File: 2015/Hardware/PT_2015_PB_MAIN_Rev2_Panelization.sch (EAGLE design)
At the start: 161 parts, among them Q1 Q_ACS711LC_SKETCH, Q11 Q_IRFS7437PbF, Q12 2N7002, Q14 Q_IRFS7437PbF, Q16 Q_IRFS7437PbF, Q18 Q_FDT86102LZ, Q20 Q_IRFS7437PbF, Q4 Q_ACS711LC, Q5 Q_ACS711LC, Q6 Q_IRFS7437PbF, Q7 Q_IRFS7437PbF, Q9 Q_IRFS7437PbF

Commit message: Fixed the Ferrite Bead Footprint
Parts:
- L3: device resistor:L-USL3216C -> rcl:L-USL4532C
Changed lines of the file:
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@@
 <part name="GND30" library="SparkFun-Aesthetics" deviceset="GND" device=""/>
 <part name="C17" library="resistor" deviceset="C-US" device="C1206" value="47µF"/>
-<part name="L3" library="resistor" deviceset="L-US" device="L3216C"/>
 <part name="C18" library="resistor" deviceset="C-US" device="C1206" value="47µF"/>
 <part name="GND31" library="SparkFun-Aesthetics" deviceset="GND" device=""/>
@@
 <part name="GND101" library="SparkFun-Aesthetics" deviceset="GND" device=""/>
 <part name="GND102" library="SparkFun-Aesthetics" deviceset="GND" device=""/>
+<part name="L3" library="rcl" deviceset="L-US" device="L4532C"/>
 </parts>
 <sheets>
@@
 <instance part="GND30" gate="1" x="218.44" y="116.84"/>
 <instance part="C17" gate="G$1" x="231.14" y="127"/>
-<instance part="L3" gate="G$1" x="241.3" y="129.54" rot="R90"/>
 <instance part="C18" gate="G$1" x="251.46" y="127"/>
 <instance part="GND31" gate="1" x="251.46" y="116.84"/>
@@
 <instance part="SG1" gate="G$1" x="-297.18" y="-165.1"/>
 <instance part="GND93" gate="1" x="-289.56" y="-180.34" rot="MR0"/>
+<instance part="L3" gate="G$1" x="241.3" y="129.54" rot="R90"/>
 </instances>
 <busses>
@@
 </segment>
 <segment>
-<pinref part="L3" gate="G$1" pin="2"/>
 <pinref part="C18" gate="G$1" pin="1"/>
 <wire x1="251.46" y1="129.54" x2="248.92" y2="129.54" width="0.1524" layer="91"/>
@@
 <wire x1="264.16" y1="129.54" x2="269.24" y2="129.54" width="0.1524" layer="91"/>
 <label x="269.24" y="129.54" size="1.27" layer="95" xref="yes"/>
-</segment>
-<segment>
+<pinref part="L3" gate="G$1" pin="2"/>
+</segment>
+<segment>

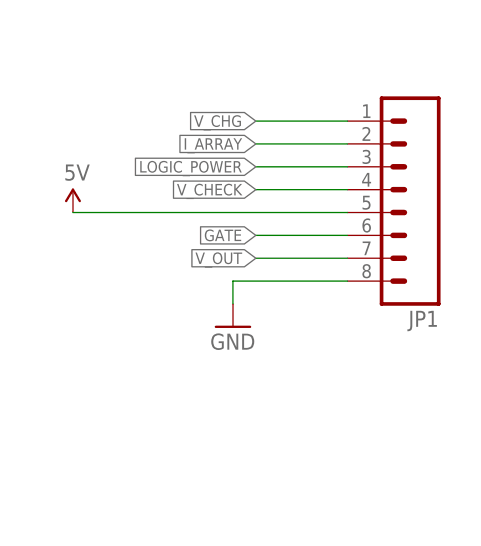
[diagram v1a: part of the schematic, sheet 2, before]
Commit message: Fixed the connector on SSR portion
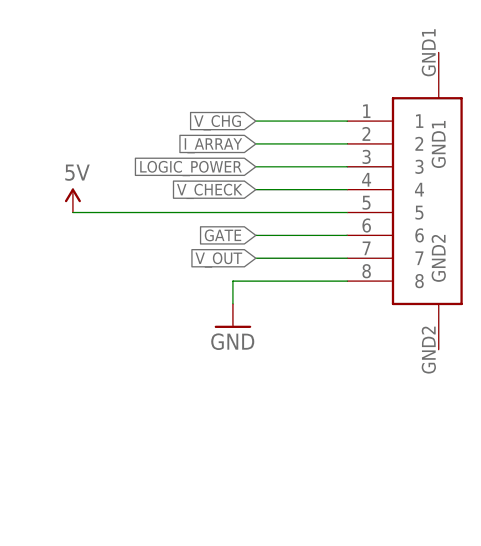
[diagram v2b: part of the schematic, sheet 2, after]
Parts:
- removed JP1: (no value), SparkFun-Connectors:M08BM08B-SRSS-TB
- added U$24: 8POS_LOGIC, New:8POS_LOGIC
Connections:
- net 5V_SSR: now also U$24.5; no longer JP1.5
- net GATE: now also U$24.6; no longer JP1.6
- net GND: now also U$24.8; no longer JP1.8
- net I_ARRAY: now also U$24.2; no longer JP1.2
- net LOGIC_POWER: now also U$24.3; no longer JP1.3
- net V_CHECK: now also U$24.4; no longer JP1.4
- net V_CHG: now also U$24.1; no longer JP1.1
- net V_OUT: now also U$24.7; no longer JP1.7
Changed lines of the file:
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@@
 <part name="D3" library="MRDT-2015-BMS" deviceset="D_STPS5045S" device=""/>
 <part name="IRLS3034-7P" library="MRDT-2015-BMS" deviceset="IRLS3034-7P" device=""/>
-<part name="JP1" library="SparkFun-Connectors" deviceset="M08" device="BM08B-SRSS-TB"/>
 <part name="SUPPLY17" library="SparkFun-Aesthetics" deviceset="5V" device=""/>
 <part name="GND100" library="SparkFun-Aesthetics" deviceset="GND" device=""/>
@@
 <part name="GND102" library="SparkFun-Aesthetics" deviceset="GND" device=""/>
 <part name="L3" library="rcl" deviceset="L-US" device="L4532C"/>
+<part name="U$24" library="New" deviceset="8POS_LOGIC" device=""/>
 </parts>
 <sheets>
@@
 <instance part="D3" gate="G$1" x="68.58" y="63.5" rot="R270"/>
 <instance part="IRLS3034-7P" gate="G$1" x="139.7" y="45.72" rot="R90"/>
-<instance part="JP1" gate="G$1" x="215.9" y="104.14" rot="R180"/>
 <instance part="SUPPLY17" gate="G$1" x="180.34" y="101.6"/>
 <instance part="GND100" gate="1" x="198.12" y="88.9"/>
@@
 <instance part="GND101" gate="1" x="116.84" y="50.8"/>
 <instance part="GND102" gate="1" x="81.28" y="50.8"/>
+<instance part="U$24" gate="G$1" x="215.9" y="96.52"/>
 </instances>
 <busses>
@@
 </segment>
 <segment>
-<pinref part="JP1" gate="G$1" pin="5"/>
 <wire x1="210.82" y1="101.6" x2="180.34" y2="101.6" width="0.1524" layer="91"/>
 <pinref part="SUPPLY17" gate="G$1" pin="5V"/>
+<pinref part="U$24" gate="G$1" pin="5"/>
 </segment>
 </net>
@@
 </segment>
 <segment>
-<pinref part="JP1" gate="G$1" pin="8"/>
 <wire x1="210.82" y1="93.98" x2="198.12" y2="93.98" width="0.1524" layer="91"/>
 <wire x1="198.12" y1="93.98" x2="198.12" y2="91.44" width="0.1524" layer="91"/>
 <pinref part="GND100" gate="1" pin="GND"/>
+<pinref part="U$24" gate="G$1" pin="8"/>
 </segment>
 <segment>
@@
 </segment>
 <segment>
-<pinref part="JP1" gate="G$1" pin="6"/>
 <wire x1="210.82" y1="99.06" x2="200.66" y2="99.06" width="0.1524" layer="91"/>
 <label x="200.66" y="99.06" size="1.27" layer="95" rot="R180" xref="yes"/>
+<pinref part="U$24" gate="G$1" pin="6"/>
 </segment>
 </net>
@@
 </segment>
 <segment>
-<pinref part="JP1" gate="G$1" pin="2"/>
 <wire x1="210.82" y1="109.22" x2="200.66" y2="109.22" width="0.1524" layer="91"/>
 <label x="200.66" y="109.22" size="1.27" layer="95" rot="R180" xref="yes"/>
+<pinref part="U$24" gate="G$1" pin="2"/>
 </segment>
 </net>
@@
 </segment>
 <segment>
-<pinref part="JP1" gate="G$1" pin="7"/>
 <wire x1="210.82" y1="96.52" x2="200.66" y2="96.52" width="0.1524" layer="91"/>
 <label x="200.66" y="96.52" size="1.27" layer="95" rot="R180" xref="yes"/>
+<pinref part="U$24" gate="G$1" pin="7"/>
 </segment>
 </net>
@@
 </segment>
 <segment>
-<pinref part="JP1" gate="G$1" pin="4"/>
 <wire x1="210.82" y1="104.14" x2="200.66" y2="104.14" width="0.1524" layer="91"/>
 <label x="200.66" y="104.14" size="1.27" layer="95" rot="R180" xref="yes"/>
+<pinref part="U$24" gate="G$1" pin="4"/>
 </segment>
 </net>
@@
 </segment>
 <segment>
-<pinref part="JP1" gate="G$1" pin="1"/>
 <wire x1="210.82" y1="111.76" x2="200.66" y2="111.76" width="0.1524" layer="91"/>
 <label x="200.66" y="111.76" size="1.27" layer="95" rot="R180" xref="yes"/>
+<pinref part="U$24" gate="G$1" pin="1"/>
 </segment>
 </net>
@@
 </segment>
 <segment>
-<pinref part="JP1" gate="G$1" pin="3"/>
 <wire x1="210.82" y1="106.68" x2="200.66" y2="106.68" width="0.1524" layer="91"/>
 <label x="200.66" y="106.68" size="1.27" layer="95" rot="R180" xref="yes"/>
-</segment>
-</net>
+<pinref part="U$24" gate="G$1" pin="3"/>
+</segment>
+</net>

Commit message: Switched out the SSR to meet 3oz Spec
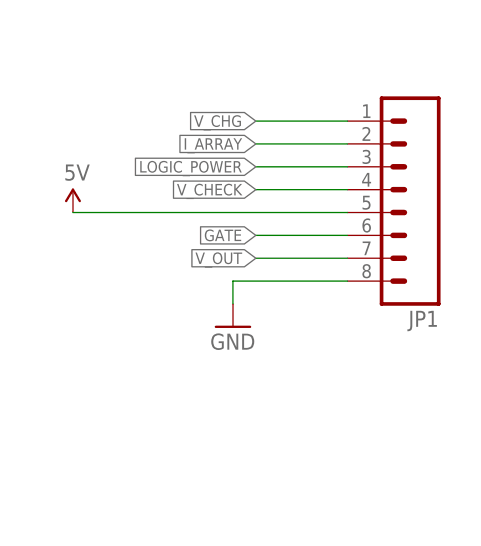
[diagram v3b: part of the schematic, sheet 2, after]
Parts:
- removed U$24: 8POS_LOGIC, New:8POS_LOGIC
- added JP1: (no value), SparkFun-Connectors:M08BM08B-SRSS-TB
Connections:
- removed net GND: 12V-AUX.L, 12V-CRIT.L, 5V-EXT.L, 5V-INT.L, ARM_P.L, AUX_P.L, BATT-NEG.P$1, C1.-, C10.1, C11.2, C12.2, C13.1, C14.1, C15.1, C16.1, C17.2, C18.2, C19.2, C2.-, C20.2, C21.-, C22.-, C23.1, C24.1, C25.1, C26.1, C27.2, C28.1, C29.1, C3.-, C30.1, C31.2, C32.1, C33.1, C34.1, C35.2, C36.1, C37.2, C38.2, C39.1, C4.-, C40.2, C41.1, C42.2, C43.2, C44.2, C45.-, C46.2, C5.1, C6.1, C7.2, C8.2, C9.2, CHARGER_IN.R, D1.A, D2.A, DOOKU-12V-CRIT.GND, DOOKU-12V-CRIT.GND1, LED1.C, LED10.C, LED11.C, LED12.C, LED13.C, LED14.C, LED2.C, LED3.C, LED4.C, LED5.C, LED6.C, LED7.C, LED8.C, LED9.C, MOTOR_1.L, MOTOR_2.L, MOTOR_3.L, MOTOR_4.L, MOTOR_5.L, MOTOR_6.L, OKI-78SR-5/1.5-W36H.GND, PALPATINE-12V.-VIN, PALPATINE-12V.-VOUT, Q1.GND, Q12.S, Q4.GND, Q5.GND, R17.2, R19.2, R23.2, R27.1, R4.1, R7.1, R8.1, SG1.1, SIDEOUS-12V.-VIN, SIDEOUS-12V.-VOUT, U$1.GND@1, U$1.GND@2, U$10.GND, U$11.GND, U$12.GND, U$13.GND, U$14.GND, U$15.GND, U$16.GND, U$17.GND, U$18.GND, U$19.GND, U$2.A, U$20.GND, U$21.GND, U$22.GND, U$23.GND, U$24.8, U$3.GND, U$4.7, U$4.8, U$5.A, U$6.GND, U$7.GND, U$8.GND, U$9.GND, VADER-5V-EXT.GND, VADER-5V-EXT.GND1
- new net 0: 12V-AUX.L, 12V-CRIT.L, 5V-EXT.L, 5V-INT.L, ARM_P.L, AUX_P.L, BATT-NEG.P$1, C1.-, C10.1, C11.2, C12.2, C13.1, C14.1, C15.1, C16.1, C17.2, C18.2, C19.2, C2.-, C20.2, C21.-, C22.-, C23.1, C24.1, C25.1, C26.1, C27.2, C28.1, C29.1, C3.-, C30.1, C31.2, C32.1, C33.1, C34.1, C35.2, C36.1, C37.2, C38.2, C39.1, C4.-, C40.2, C41.1, C42.2, C43.2, C44.2, C45.-, C5.1, C6.1, C7.2, C8.2, C9.2, D1.A, D2.A, DOOKU-12V-CRIT.GND, DOOKU-12V-CRIT.GND1, LED1.C, LED10.C, LED11.C, LED12.C, LED13.C, LED14.C, LED2.C, LED3.C, LED4.C, LED5.C, LED6.C, LED7.C, LED8.C, LED9.C, MOTOR_1.L, MOTOR_2.L, MOTOR_3.L, MOTOR_4.L, MOTOR_5.L, MOTOR_6.L, OKI-78SR-5/1.5-W36H.GND, PALPATINE-12V.-VIN, PALPATINE-12V.-VOUT, Q1.GND, Q12.S, Q4.GND, Q5.GND, R4.1, R7.1, R8.1, SG1.1, SIDEOUS-12V.-VIN, SIDEOUS-12V.-VOUT, U$1.GND@1, U$1.GND@2, U$10.GND, U$11.GND, U$12.GND, U$13.GND, U$14.GND, U$15.GND, U$16.GND, U$17.GND, U$18.GND, U$19.GND, U$2.A, U$20.GND, U$21.GND, U$3.GND, U$4.7, U$4.8, U$5.A, U$6.GND, U$7.GND, U$8.GND, U$9.GND, VADER-5V-EXT.GND, VADER-5V-EXT.GND1
- new net GND_SSR: C46.2, CHARGER_IN.R, JP1.8, R17.2, R19.2, R23.2, R27.1, U$22.GND, U$23.GND
- net 5V_SSR: now also JP1.5; no longer U$24.5
- net GATE: now also JP1.6; no longer U$24.6
- net I_ARRAY: now also JP1.2; no longer U$24.2
- net LOGIC_POWER: now also JP1.3; no longer U$24.3
- net V_CHECK: now also JP1.4; no longer U$24.4
- net V_CHG: now also JP1.1; no longer U$24.1
- net V_OUT: now also JP1.7; no longer U$24.7
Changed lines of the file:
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@@
 <part name="SG1" library="SparkFun-Electromechanical" deviceset="BUZZER" device="SMD2"/>
 <part name="GND93" library="SparkFun-Aesthetics" deviceset="GND" device=""/>
+<part name="L3" library="rcl" deviceset="L-US" device="L4532C"/>
 <part name="U$22" library="MRDT-2015-BMS" deviceset="ACS770" device=""/>
 <part name="IRLS3034-7P.2" library="MRDT-2015-BMS" deviceset="IRLS3034-7P" device=""/>
@@
 <part name="D3" library="MRDT-2015-BMS" deviceset="D_STPS5045S" device=""/>
 <part name="IRLS3034-7P" library="MRDT-2015-BMS" deviceset="IRLS3034-7P" device=""/>
+<part name="JP1" library="SparkFun-Connectors" deviceset="M08" device="BM08B-SRSS-TB"/>
 <part name="SUPPLY17" library="SparkFun-Aesthetics" deviceset="5V" device=""/>
 <part name="GND100" library="SparkFun-Aesthetics" deviceset="GND" device=""/>
@@
 <part name="GND101" library="SparkFun-Aesthetics" deviceset="GND" device=""/>
 <part name="GND102" library="SparkFun-Aesthetics" deviceset="GND" device=""/>
-<part name="L3" library="rcl" deviceset="L-US" device="L4532C"/>
-<part name="U$24" library="New" deviceset="8POS_LOGIC" device=""/>
 </parts>
 <sheets>
@@
 </busses>
 <nets>
-<net name="GND" class="0">
+<net name="0" class="0">
 <segment>
 <pinref part="DOOKU-12V-CRIT" gate="G$1" pin="GND"/>
@@
 <instance part="D3" gate="G$1" x="68.58" y="63.5" rot="R270"/>
 <instance part="IRLS3034-7P" gate="G$1" x="139.7" y="45.72" rot="R90"/>
+<instance part="JP1" gate="G$1" x="215.9" y="104.14" rot="R180"/>
 <instance part="SUPPLY17" gate="G$1" x="180.34" y="101.6"/>
 <instance part="GND100" gate="1" x="198.12" y="88.9"/>
@@
 <instance part="GND101" gate="1" x="116.84" y="50.8"/>
 <instance part="GND102" gate="1" x="81.28" y="50.8"/>
-<instance part="U$24" gate="G$1" x="215.9" y="96.52"/>
 </instances>
 <busses>
 </busses>
 <nets>
-<net name="N$354" class="0">
+<net name="N$33" class="0">
 <segment>
 <pinref part="IRLS3034-7P.2" gate="G$1" pin="SOURCE"/>
@@
 </segment>
 <segment>
+<pinref part="JP1" gate="G$1" pin="5"/>
 <wire x1="210.82" y1="101.6" x2="180.34" y2="101.6" width="0.1524" layer="91"/>
 <pinref part="SUPPLY17" gate="G$1" pin="5V"/>
-<pinref part="U$24" gate="G$1" pin="5"/>
-</segment>
-</net>
-<net name="GND" class="0">
+</segment>
+</net>
+<net name="GND_SSR" class="0">
 <segment>
 <pinref part="U$22" gate="G$1" pin="GND"/>
@@
 </segment>
 <segment>
+<pinref part="JP1" gate="G$1" pin="8"/>
 <wire x1="210.82" y1="93.98" x2="198.12" y2="93.98" width="0.1524" layer="91"/>
 <wire x1="198.12" y1="93.98" x2="198.12" y2="91.44" width="0.1524" layer="91"/>
 <pinref part="GND100" gate="1" pin="GND"/>
-<pinref part="U$24" gate="G$1" pin="8"/>
 </segment>
 <segment>
@@
 </segment>
 </net>
-<net name="N$355" class="0">
+<net name="N$354" class="0">
 <segment>
 <pinref part="U$23" gate="G$1" pin="GATE"/>
@@
 </segment>
 <segment>
+<pinref part="JP1" gate="G$1" pin="6"/>
 <wire x1="210.82" y1="99.06" x2="200.66" y2="99.06" width="0.1524" layer="91"/>
 <label x="200.66" y="99.06" size="1.27" layer="95" rot="R180" xref="yes"/>
-<pinref part="U$24" gate="G$1" pin="6"/>
 </segment>
 </net>
@@
 </segment>
 <segment>
+<pinref part="JP1" gate="G$1" pin="2"/>
 <wire x1="210.82" y1="109.22" x2="200.66" y2="109.22" width="0.1524" layer="91"/>
 <label x="200.66" y="109.22" size="1.27" layer="95" rot="R180" xref="yes"/>
-<pinref part="U$24" gate="G$1" pin="2"/>
 </segment>
 </net>
@@
 </segment>
 <segment>
+<pinref part="JP1" gate="G$1" pin="7"/>
 <wire x1="210.82" y1="96.52" x2="200.66" y2="96.52" width="0.1524" layer="91"/>
 <label x="200.66" y="96.52" size="1.27" layer="95" rot="R180" xref="yes"/>
-<pinref part="U$24" gate="G$1" pin="7"/>
-</segment>
-</net>
-<net name="N$356" class="0">
+</segment>
+</net>
+<net name="N$355" class="0">
 <segment>
 <pinref part="U$22" gate="G$1" pin="IP+"/>
@@
 </segment>
 </net>
-<net name="N$357" class="0">
+<net name="N$356" class="0">
 <segment>
 <pinref part="C46" gate="G$1" pin="1"/>
@@
 </segment>
 </net>
-<net name="N$358" class="0">
+<net name="N$357" class="0">
 <segment>
 <pinref part="S1" gate="1" pin="S"/>
@@
 </segment>
 <segment>
+<pinref part="JP1" gate="G$1" pin="4"/>
 <wire x1="210.82" y1="104.14" x2="200.66" y2="104.14" width="0.1524" layer="91"/>
 <label x="200.66" y="104.14" size="1.27" layer="95" rot="R180" xref="yes"/>
-<pinref part="U$24" gate="G$1" pin="4"/>
 </segment>
 </net>
@@
 </segment>
 <segment>
+<pinref part="JP1" gate="G$1" pin="1"/>
 <wire x1="210.82" y1="111.76" x2="200.66" y2="111.76" width="0.1524" layer="91"/>
 <label x="200.66" y="111.76" size="1.27" layer="95" rot="R180" xref="yes"/>
-<pinref part="U$24" gate="G$1" pin="1"/>
-</segment>
-</net>
-<net name="N$359" class="0">
+</segment>
+</net>
+<net name="N$358" class="0">
 <segment>
 <pinref part="R25" gate="G$1" pin="2"/>
@@
 </segment>
 <segment>
+<pinref part="JP1" gate="G$1" pin="3"/>
 <wire x1="210.82" y1="106.68" x2="200.66" y2="106.68" width="0.1524" layer="91"/>
 <label x="200.66" y="106.68" size="1.27" layer="95" rot="R180" xref="yes"/>
-<pinref part="U$24" gate="G$1" pin="3"/>
-</segment>
-</net>
+</segment>
+</net>
